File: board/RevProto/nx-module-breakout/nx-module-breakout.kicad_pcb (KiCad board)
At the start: 4 copper layers, 69.9 x 54 mm, 58 parts, among them J1 Conn_02x15_Odd_Even, J10 FTSH-105-01-L-DV-007-K, J2 DF40C-60DS-0.4V(51), J3 Conn_02x15_Odd_Even, J4 Conn_02x15_Odd_Even, J5 DF40C-60DS-0.4V(51), J6 SFV22R-2STE1HLF, J7 SFV22R-2STE1HLF, J8 Conn_02x06_Odd_Even, J9 USB_C_Receptacle_USB2.0_14P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

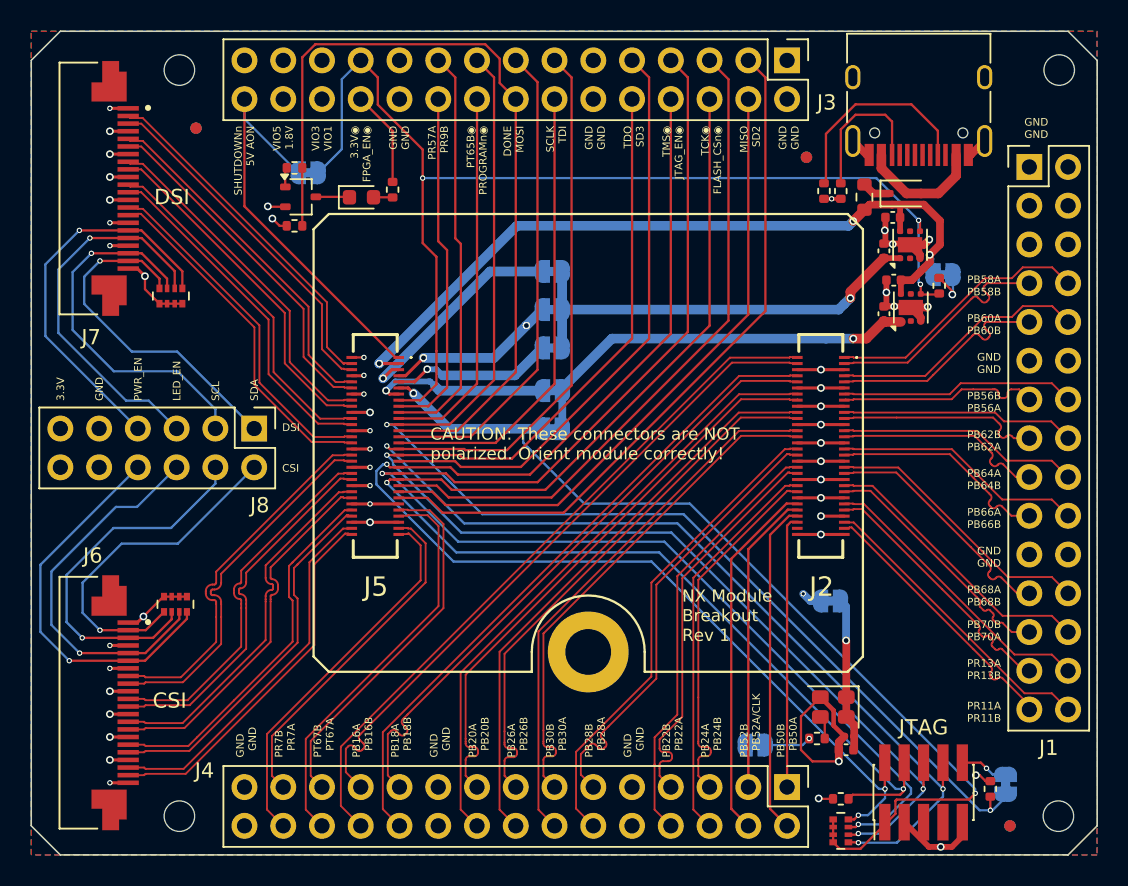
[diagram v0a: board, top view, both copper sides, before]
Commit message: Breakout: 100 ohm differential pairs consistently have 8 mil spacing
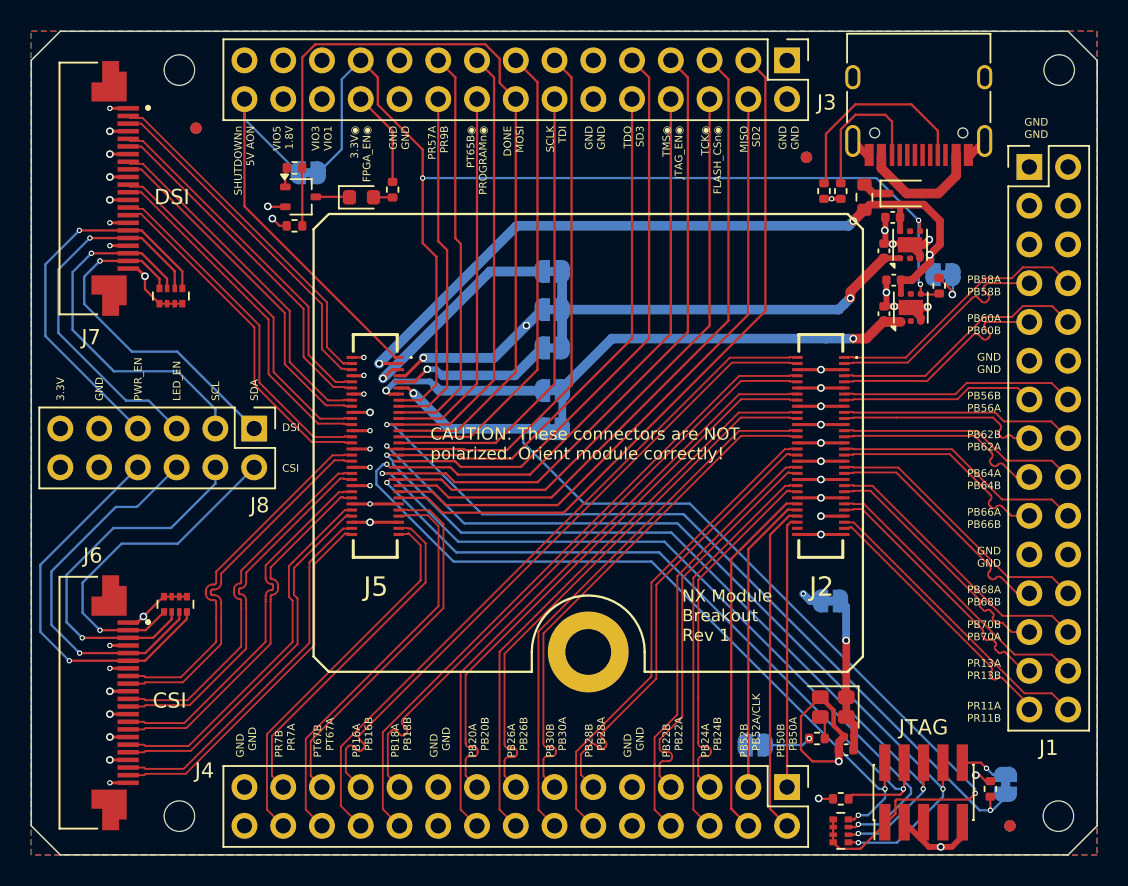
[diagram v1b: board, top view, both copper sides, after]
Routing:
- net /PB56N: track 13.4 -> 12.8 mm
